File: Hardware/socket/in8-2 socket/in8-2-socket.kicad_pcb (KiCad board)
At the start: 2 copper layers, 105 x 40 mm, 19 parts, among them J3 Conn_01x20_Male, Q1 BC847BS, Q2 BC847BS

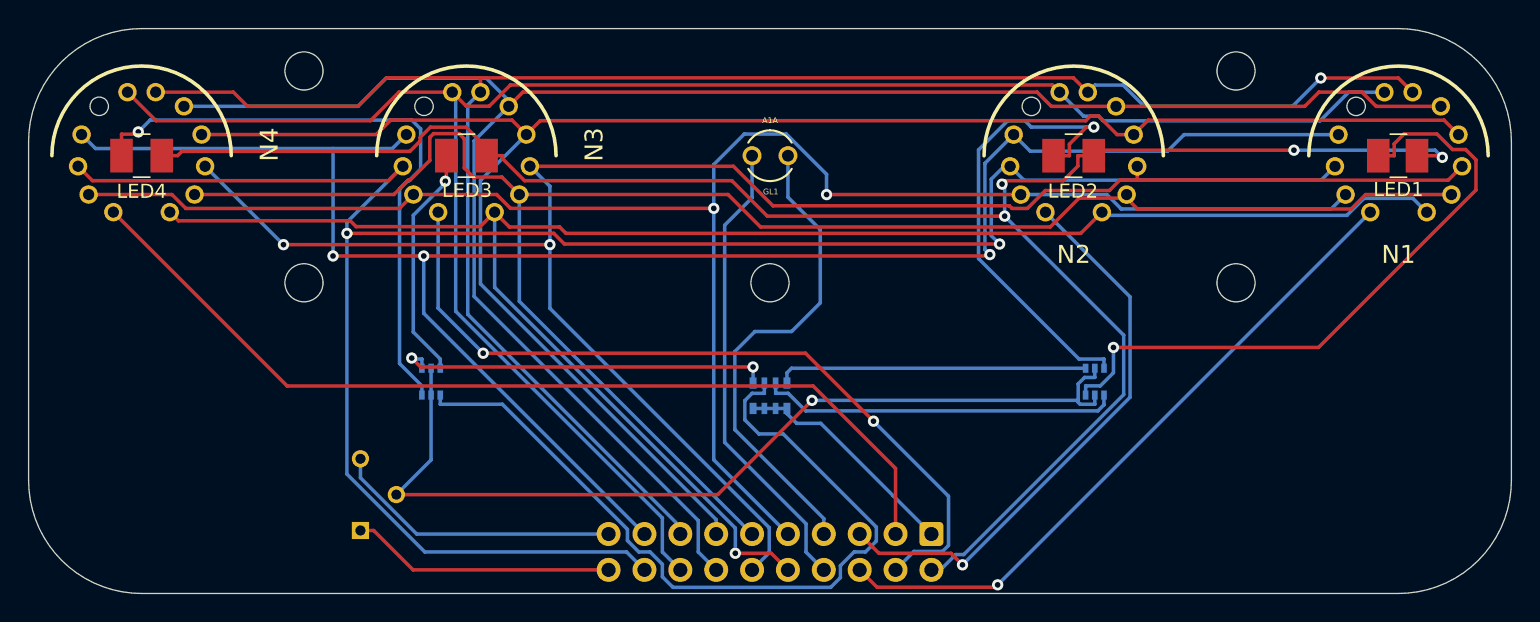
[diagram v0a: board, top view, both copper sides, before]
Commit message: fix switch pin assignment, reduce hole size on nixie sockets
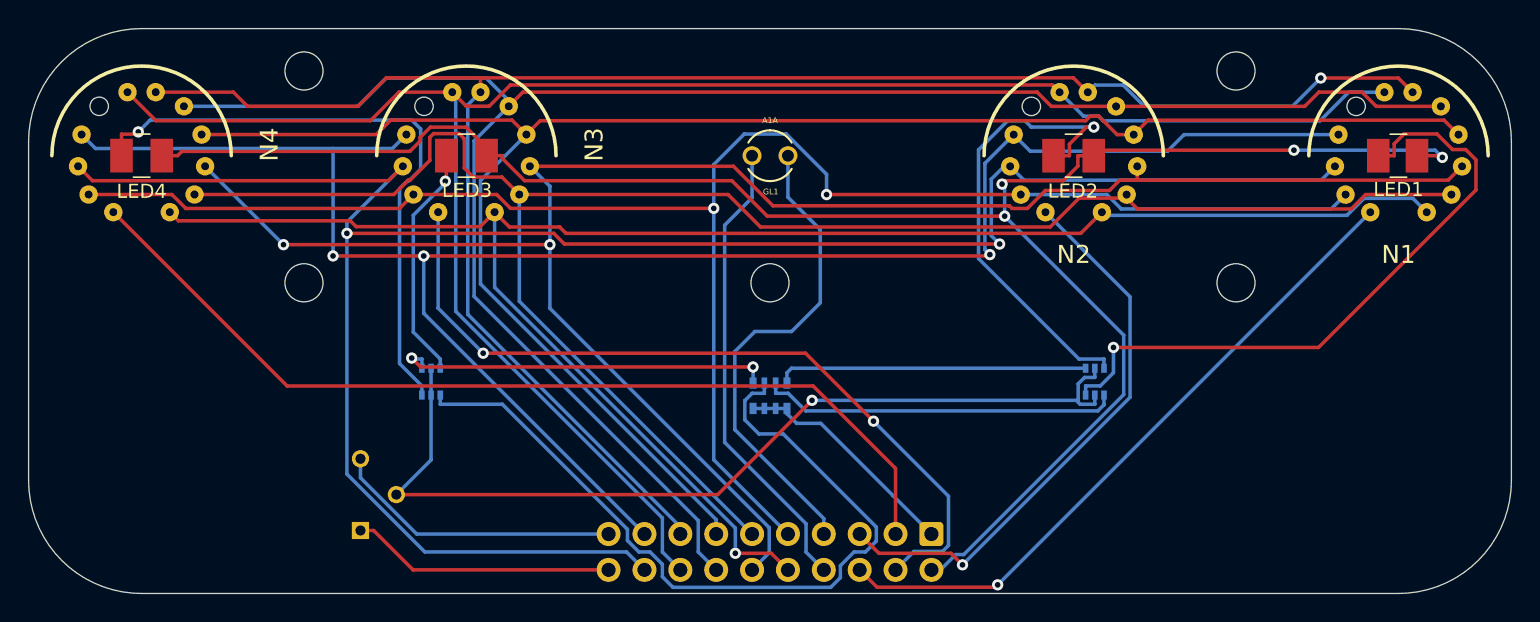
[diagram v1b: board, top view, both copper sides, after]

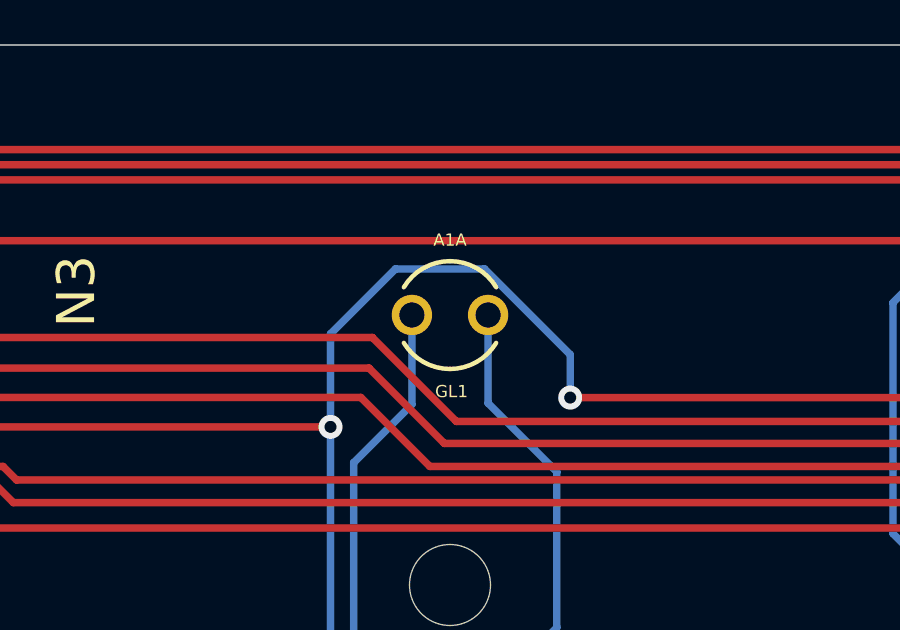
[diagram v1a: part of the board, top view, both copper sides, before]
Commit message: add battery backup for power failures
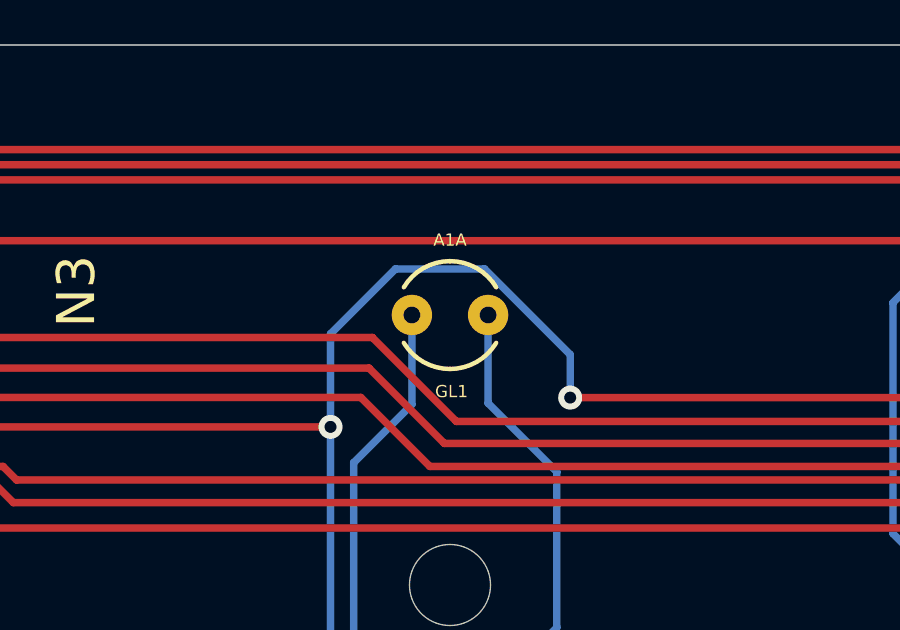
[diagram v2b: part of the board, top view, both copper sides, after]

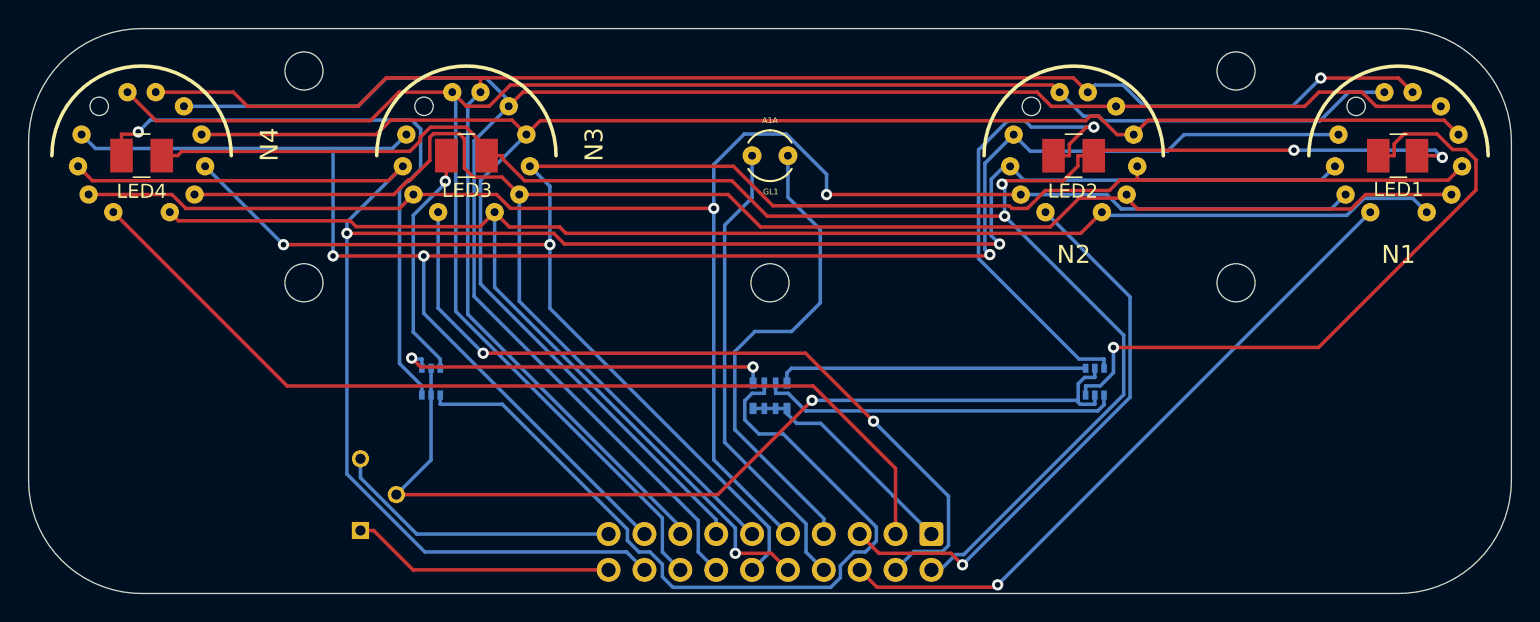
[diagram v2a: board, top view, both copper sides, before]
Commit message: relocate libraries for socket boards, fix routing & 3D models
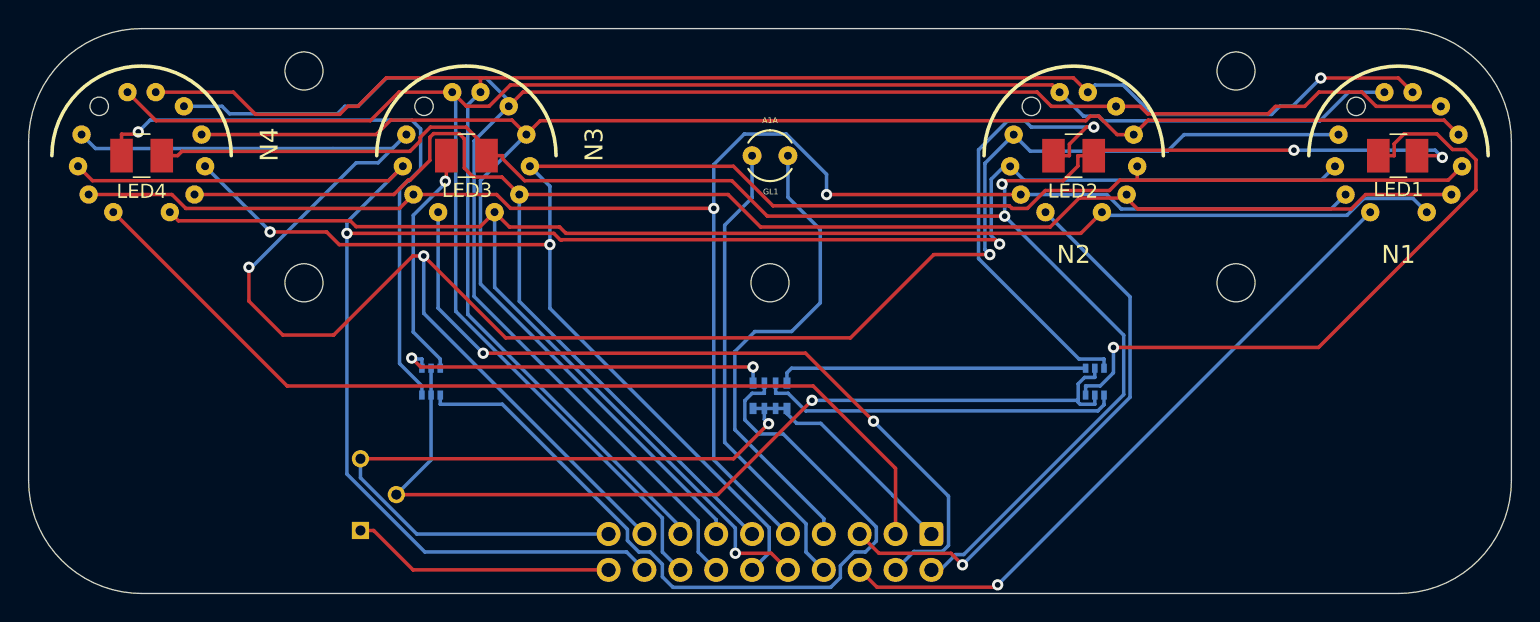
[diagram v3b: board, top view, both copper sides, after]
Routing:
- net GND: track 37.1 -> 68.2 mm, vias 0 -> 1
- net Net-(J3-Pad17): track 137.6 -> 160.3 mm
- net Net-(J3-Pad15): track 131.7 -> 132.6 mm
- net Net-(J3-Pad14): track 133.5 -> 134.4 mm
